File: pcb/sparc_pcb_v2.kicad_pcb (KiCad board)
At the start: 2 copper layers, 36.5 x 36.5 mm, 19 parts, among them SW4 Reset, SW5 BOOT, U2 ESP32-WROOM-32

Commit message: placing C8, R8, and R9
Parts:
- added C8: 1µF, Capacitor_SMD:C_1206_3216Metric_Pad1.33x1.80mm_HandSolder, B.Cu at (144.4, 77.5)
- added R8: 4.7k, Resistor_SMD:R_1206_3216Metric_Pad1.30x1.75mm_HandSolder, B.Cu at (122.0, 98.5)
- added R9: 4.7k, Resistor_SMD:R_1206_3216Metric_Pad1.30x1.75mm_HandSolder, B.Cu at (121.5, 95.0)
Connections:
- LDO1 pad 3: unconnected-(LDO1-EN-Pad3) -> TP4056 OUT+
- SW4 pad 2: +3.3V -> Net-(U2-EN)
- SW5 pad 2: +3.3V -> Net-(U2-IO0)
- VL53L0X1 pad 3: Net-(U2-IO16) -> Net-(U2-IO17)
- VL53L0X1 pad 4: Net-(U2-IO17) -> Net-(U2-IO16)

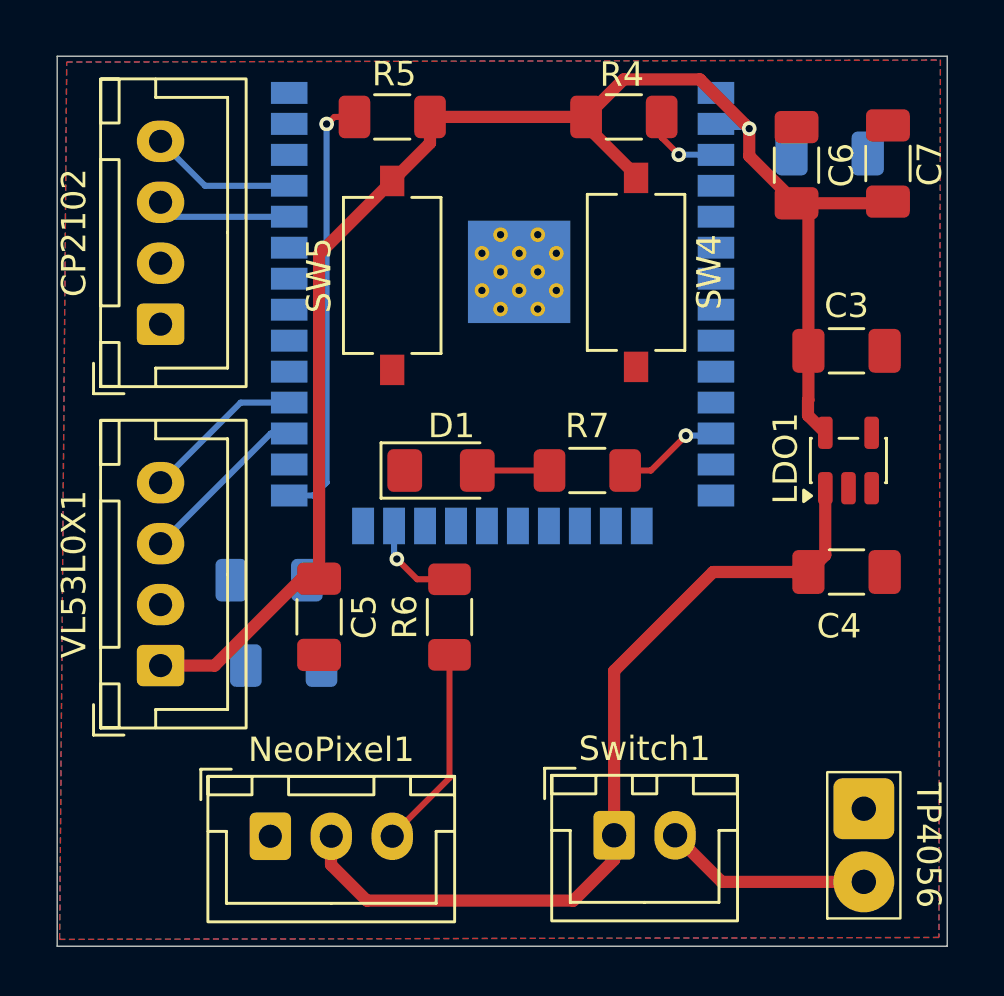
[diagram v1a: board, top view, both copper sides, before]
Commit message: fixed sw4 and sw5 wiring on the pcb
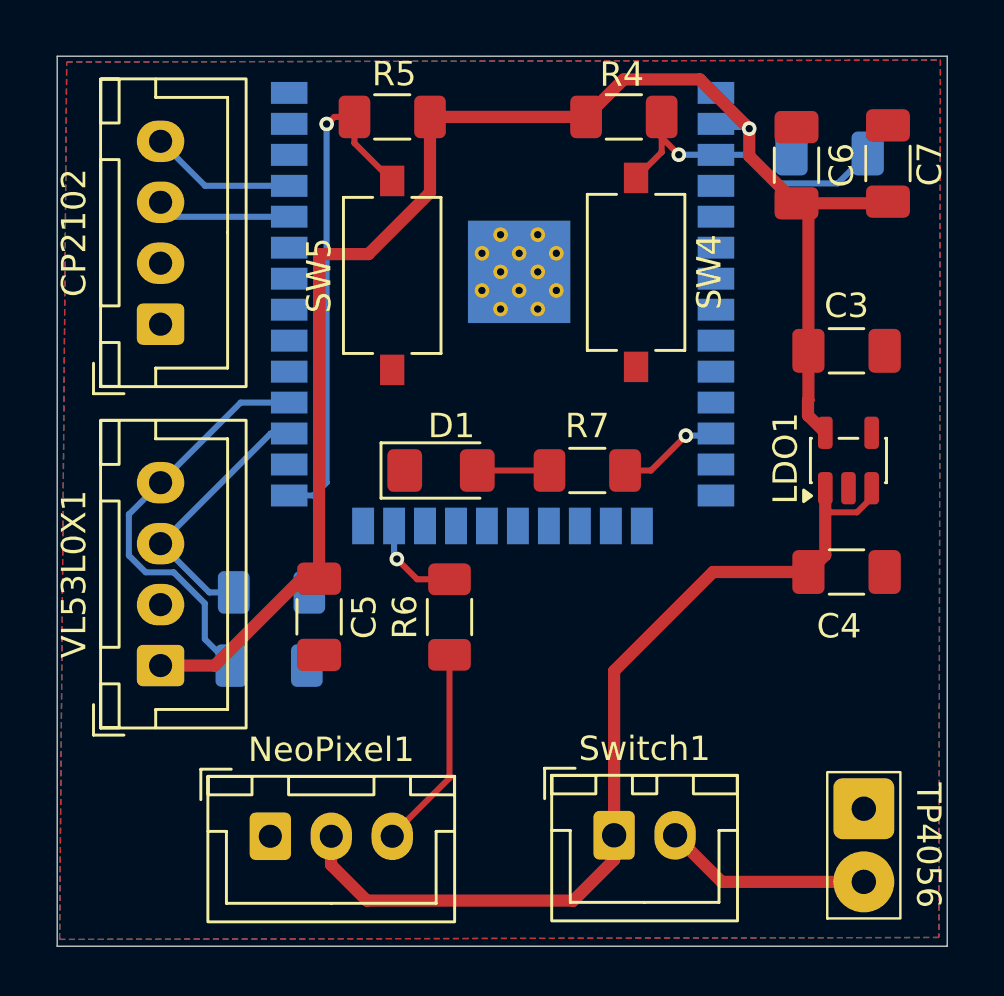
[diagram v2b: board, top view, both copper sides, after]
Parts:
- moved R8 0.60 mm to (121.5, 98.5)
- moved R9 0.51 mm to (121.5, 95.5)
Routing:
- net Net-(U2-IO16): track 7.15 -> 17.1 mm
- net Net-(U2-EN): track 3.57 -> 13.0 mm
- net TP4056 OUT+: track 35.2 -> 38.6 mm
- net Net-(U2-IO17): track 6.64 -> 10.0 mm
- net Net-(U2-IO0): track 18.0 -> 20.7 mm
- net +3.3V: track 65.7 -> 63.9 mm
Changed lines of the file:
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@@
 	(footprint "Resistor_SMD:R_1206_3216Metric_Pad1.30x1.75mm_HandSolder"
 		(layer "B.Cu")
-		(at 121.45 95 180)
+		(at 121.55 95.5 180)
 		(descr "Resistor SMD 1206 (3216 Metric), square (rectangular) end terminal, IPC-7351 nominal with elongated pad for handsoldering. (Body size source: IPC-SM-782 page 72, https://www.pcb-3d.com/wordpress/wp-content/uploads/ipc-sm-782a_amendment_1_and_2.pdf)")
 		(tags "resistor handsolder")
@@
 	(footprint "Resistor_SMD:R_1206_3216Metric_Pad1.30x1.75mm_HandSolder"
 		(layer "B.Cu")
-		(at 122.05 98.5 180)
+		(at 121.45 98.5 180)
 		(descr "Resistor SMD 1206 (3216 Metric), square (rectangular) end terminal, IPC-7351 nominal with elongated pad for handsoldering. (Body size source: IPC-SM-782 page 72, https://www.pcb-3d.com/wordpress/wp-content/uploads/ipc-sm-782a_amendment_1_and_2.pdf)")
 		(tags "resistor handsolder")
@@
 	)
 	(segment
+		(start 128.05 79.1)
+		(end 125.525 81.625)
+		(width 0.5)
+		(layer "F.Cu")
+		(net "+3.3V")
+	)
+	(segment
 		(start 144.26 88.9525)
 		(end 143.55 88.2425)
@@
 	)
 	(segment
-		(start 128.05 77.075)
-		(end 126.5 78.625)
-		(width 0.5)
-		(layer "F.Cu")
-		(net "+3.3V")
-	)
-	(segment
 		(start 143.5675 80.03)
 		(end 143.08 79.5425)
@@
 	)
 	(segment
-		(start 128.05 76)
-		(end 128.05 77.075)
-		(width 0.5)
-		(layer "F.Cu")
-		(net "+3.3V")
-	)
-	(segment
 		(start 122.7825 94.9375)
 		(end 119.22 98.5)
@@
 	)
 	(segment
-		(start 126.5 78.625)
-		(end 123.5 81.625)
-		(width 0.5)
-		(layer "F.Cu")
-		(net "+3.3V")
-	)
-	(segment
 		(start 146.76 79.5425)
 		(end 146.83 79.4725)
@@
 	)
 	(segment
-		(start 136.48 78.38)
-		(end 134.45 76.35)
-		(width 0.5)
-		(layer "F.Cu")
-		(net "+3.3V")
-	)
-	(segment
-		(start 136.48 78.48)
-		(end 136.48 78.38)
-		(width 0.25)
+		(start 125.525 81.625)
+		(end 123.5 81.625)
+		(width 0.5)
 		(layer "F.Cu")
 		(net "+3.3V")
@@
 	)
 	(segment
+		(start 128.05 76)
+		(end 128.05 79.1)
+		(width 0.5)
+		(layer "F.Cu")
+		(net "+3.3V")
+	)
+	(segment
 		(start 135.988279 74.461721)
 		(end 139.121721 74.461721)
@@
 		(end 117 98.5)
 		(width 0.5)
-		(layer "F.Cu")
-		(net "+3.3V")
-	)
-	(segment
-		(start 136.5 78.5)
-		(end 136.48 78.48)
-		(width 0.25)
 		(layer "F.Cu")
 		(net "+3.3V")
@@
 	)
 	(segment
+		(start 144.26 92)
+		(end 144.26 91.2275)
+		(width 0.25)
+		(layer "F.Cu")
+		(net "TP4056 OUT+")
+	)
+	(segment
 		(start 133.93 108.14)
 		(end 125.46 108.14)
@@
 	)
 	(segment
+		(start 146.16 91.615908)
+		(end 145.560908 92.215)
+		(width 0.25)
+		(layer "F.Cu")
+		(net "TP4056 OUT+")
+	)
+	(segment
+		(start 146.16 91.2275)
+		(end 146.16 91.615908)
+		(width 0.25)
+		(layer "F.Cu")
+		(net "TP4056 OUT+")
+	)
+	(segment
 		(start 143.5675 94.6625)
 		(end 139.6575 94.6625)
@@
 	)
 	(segment
+		(start 144.475 92.215)
+		(end 144.26 92)
+		(width 0.25)
+		(layer "F.Cu")
+		(net "TP4056 OUT+")
+	)
+	(segment
 		(start 135.6 106.47)
 		(end 133.93 108.14)
@@
 	)
 	(segment
+		(start 145.560908 92.215)
+		(end 144.475 92.215)
+		(width 0.25)
+		(layer "F.Cu")
+		(net "TP4056 OUT+")
+	)
+	(segment
 		(start 135.6 98.72)
 		(end 135.6 105.46)
@@
 	)
 	(segment
+		(start 136.48 78.48)
+		(end 136.48 78.38)
+		(width 0.25)
+		(layer "F.Cu")
+		(net "Net-(U2-EN)")
+	)
+	(segment
+		(start 136.5 78.5)
+		(end 137.55 77.45)
+		(width 0.25)
+		(layer "F.Cu")
+		(net "Net-(U2-EN)")
+	)
+	(segment
+		(start 137.55 77.45)
+		(end 137.55 76.85)
+		(width 0.25)
+		(layer "F.Cu")
+		(net "Net-(U2-EN)")
+	)
+	(segment
 		(start 137.55 76.85)
 		(end 138.25 77.55)
+		(width 0.25)
+		(layer "F.Cu")
+		(net "Net-(U2-EN)")
+	)
+	(segment
+		(start 136.5 78.5)
+		(end 136.48 78.48)
 		(width 0.25)
 		(layer "F.Cu")
@@
 	)
 	(segment
+		(start 141.0474 77.555)
+		(end 139.775 77.555)
+		(width 0.25)
+		(layer "B.Cu")
+		(net "Net-(U2-EN)")
+	)
+	(segment
 		(start 139.77 77.55)
 		(end 139.775 77.555)
@@
 		(start 138.25 77.55)
 		(end 139.77 77.55)
+		(width 0.25)
+		(layer "B.Cu")
+		(net "Net-(U2-EN)")
+	)
+	(segment
+		(start 144.775 78.725)
+		(end 142.2174 78.725)
+		(width 0.25)
+		(layer "B.Cu")
+		(net "Net-(U2-EN)")
+	)
+	(segment
+		(start 142.2174 78.725)
+		(end 141.0474 77.555)
+		(width 0.25)
+		(layer "B.Cu")
+		(net "Net-(U2-EN)")
+	)
+	(segment
+		(start 146 77.5)
+		(end 144.775 78.725)
 		(width 0.25)
 		(layer "B.Cu")
@@
 	)
 	(segment
+		(start 119.9 98.5)
+		(end 118.813604 97.413604)
+		(width 0.25)
+		(layer "B.Cu")
+		(net "Net-(U2-IO16)")
+	)
+	(segment
+		(start 117.538604 94.675)
+		(end 116.388299 94.675)
+		(width 0.25)
+		(layer "B.Cu")
+		(net "Net-(U2-IO16)")
+	)
+	(segment
+		(start 115.7 93.986701)
+		(end 115.7 92.3)
+		(width 0.25)
+		(layer "B.Cu")
+		(net "Net-(U2-IO16)")
+	)
+	(segment
+		(start 115.7 92.3)
+		(end 116.681802 91.318198)
+		(width 0.25)
+		(layer "B.Cu")
+		(net "Net-(U2-IO16)")
+	)
+	(segment
+		(start 118.813604 95.95)
+		(end 117.538604 94.675)
+		(width 0.25)
+		(layer "B.Cu")
+		(net "Net-(U2-IO16)")
+	)
+	(segment
 		(start 117 93.5)
 		(end 121.515 88.985)
@@
 	)
 	(segment
+		(start 116.388299 94.675)
+		(end 115.7 93.986701)
+		(width 0.25)
+		(layer "B.Cu")
+		(net "Net-(U2-IO16)")
+	)
+	(segment
+		(start 118.813604 97.413604)
+		(end 118.813604 95.95)
+		(width 0.25)
+		(layer "B.Cu")
+		(net "Net-(U2-IO16)")
+	)
+	(segment
 		(start 117 91)
 		(end 120.285 87.715)
@@
 	)
 	(segment
+		(start 119 95.5)
+		(end 117.318198 93.818198)
+		(width 0.25)
+		(layer "B.Cu")
+		(net "Net-(U2-IO17)")
+	)
+	(segment
 		(start 120.285 87.715)
 		(end 122.275 87.715)
+		(width 0.25)
+		(layer "B.Cu")
+		(net "Net-(U2-IO17)")
+	)
+	(segment
+		(start 120 95.5)
+		(end 119 95.5)
 		(width 0.25)
 		(layer "B.Cu")
@@
 	)
 	(segment
+		(start 124.95 77.075)
+		(end 126.093414 78.218414)
+		(width 0.25)
+		(layer "F.Cu")
+		(net "Net-(U2-IO0)")
+	)
+	(segment
 		(start 123.81 76.29)
 		(end 123.81 76.32)
@@
 		(width 0.25)
 		(layer "F.Cu")
+		(net "Net-(U2-IO0)")
+	)
+	(segment
+		(start 124.95 76)
+		(end 124.95 77.075)
+		(width 0.25)
+		(layer "F.Cu")

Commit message: new I2C tracing and pull-up resistors
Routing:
- net Net-(U2-IO17): track 10.0 -> 32.3 mm
- net +3.3V: track 63.9 -> 70.1 mm, vias 1 -> 2
- net Net-(U2-IO16): track 17.1 -> 16.1 mm
- net Net-(U2-IO0): track 20.7 -> 21.3 mm
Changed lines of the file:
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@@
 	)
 	(segment
-		(start 123.5 81.625)
+		(start 123.5 92.5)
 		(end 123.5 94.9375)
 		(width 0.5)
@@
 	)
 	(segment
+		(start 123.5 81.625)
+		(end 123.5 92.5)
+		(width 0.5)
+		(layer "F.Cu")
+		(net "+3.3V")
+	)
+	(segment
 		(start 123.5 94.9375)
 		(end 122.7825 94.9375)
@@
 		(width 0.5)
 		(layer "F.Cu")
+		(net "+3.3V")
+	)
+	(via
+		(at 123.5 92.5)
+		(size 0.6)
+		(drill 0.3)
+		(layers "F.Cu" "B.Cu")
 		(net "+3.3V")
 	)
@@
 	)
 	(segment
+		(start 123 95.6)
+		(end 123.1 95.5)
+		(width 0.25)
+		(layer "B.Cu")
+		(net "+3.3V")
+	)
+	(segment
+		(start 123 98.5)
+		(end 123 95.6)
+		(width 0.25)
+		(layer "B.Cu")
+		(net "+3.3V")
+	)
+	(segment
 		(start 140.945 76.285)
 		(end 141.14 76.48)
+		(width 0.25)
+		(layer "B.Cu")
+		(net "+3.3V")
+	)
+	(segment
+		(start 123.1 95.5)
+		(end 123.1 92.9)
+		(width 0.25)
+		(layer "B.Cu")
+		(net "+3.3V")
+	)
+	(segment
+		(start 123.1 92.9)
+		(end 123.5 92.5)
 		(width 0.25)
 		(layer "B.Cu")
@@
 	)
 	(segment
+		(start 124.95 77.075)
+		(end 126.5 78.625)
+		(width 0.25)
+		(layer "F.Cu")
+		(net "Net-(U2-IO0)")
+	)
+	(segment
+		(start 123.81 76.29)
+		(end 123.81 76.32)
+		(width 0.25)
+		(layer "F.Cu")
+		(net "Net-(U2-IO0)")
+	)
+	(segment
+		(start 123.82 76.33)
+		(end 123.82 76.31)
+		(width 0.25)
+		(layer "F.Cu")
+		(net "Net-(U2-IO0)")
+	)
+	(segment
+		(start 124.13 76)
+		(end 124.95 76)
+		(width 0.25)
+		(layer "F.Cu")
+		(net "Net-(U2-IO0)")
+	)
+	(segment
+		(start 123.82 76.31)
+		(end 124.13 76)
+		(width 0.25)
+		(layer "F.Cu")
+		(net "Net-(U2-IO0)")
+	)
+	(segment
+		(start 124.95 76)
+		(end 124.95 77.075)
+		(width 0.25)
+		(layer "F.Cu")
+		(net "Net-(U2-IO0)")
+	)
+	(segment
+		(start 123.81 76.32)
+		(end 123.82 76.33)
+		(width 0.25)
+		(layer "F.Cu")
+		(net "Net-(U2-IO0)")
+	)
+	(via
+		(at 123.81 76.29)
+		(size 0.6)
+		(drill 0.3)
+		(layers "F.Cu" "B.Cu")
+		(net "Net-(U2-IO0)")
+	)
+	(segment
+		(start 123.81 90.99)
+		(end 123.275 91.525)
+		(width 0.25)
+		(layer "B.Cu")
+		(net "Net-(U2-IO0)")
+	)
+	(segment
+		(start 123.81 76.29)
+		(end 123.81 90.99)
+		(width 0.25)
+		(layer "B.Cu")
+		(net "Net-(U2-IO0)")
+	)
+	(segment
+		(start 122.42 91.38)
+		(end 122.275 91.525)
+		(width 0.25)
+		(layer "B.Cu")
+		(net "Net-(U2-IO0)")
+	)
+	(segment
+		(start 123.275 91.525)
+		(end 122.275 91.525)
+		(width 0.25)
+		(layer "B.Cu")
+		(net "Net-(U2-IO0)")
+	)
+	(segment
+		(start 123.81 76.29)
+		(end 123.82 76.3)
+		(width 0.25)
+		(layer "B.Cu")
+		(net "Net-(U2-IO0)")
+	)
+	(segment
+		(start 117.938604 97.175)
+		(end 118.925 98.161396)
+		(width 0.25)
+		(layer "B.Cu")
+		(net "Net-(U2-IO17)")
+	)
+	(segment
+		(start 118.925 98.161396)
+		(end 118.925 99.3701)
+		(width 0.25)
+		(layer "B.Cu")
+		(net "Net-(U2-IO17)")
+	)
+	(segment
+		(start 120.5451 99.7)
+		(end 120.875 99.3701)
+		(width 0.25)
+		(layer "B.Cu")
+		(net "Net-(U2-IO17)")
+	)
+	(segment
+		(start 115.179968 95.966669)
+		(end 116.388299 97.175)
+		(width 0.25)
+		(layer "B.Cu")
+		(net "Net-(U2-IO17)")
+	)
+	(segment
+		(start 119.2549 99.7)
+		(end 120.5451 99.7)
+		(width 0.25)
+		(layer "B.Cu")
+		(net "Net-(U2-IO17)")
+	)
+	(segment
+		(start 119 95.5)
+		(end 117.318198 93.818198)
+		(width 0.25)
+		(layer "B.Cu")
+		(net "Net-(U2-IO17)")
+	)
+	(segment
+		(start 115.179968 91.033331)
+		(end 115.179968 95.966669)
+		(width 0.25)
+		(layer "B.Cu")
+		(net "Net-(U2-IO17)")
+	)
+	(segment
+		(start 120.875 99.3701)
+		(end 120.875 97.375)
+		(width 0.25)
+		(layer "B.Cu")
+		(net "Net-(U2-IO17)")
+	)
+	(segment
+		(start 118.925 99.3701)
+		(end 119.2549 99.7)
+		(width 0.25)
+		(layer "B.Cu")
+		(net "Net-(U2-IO17)")
+	)
+	(segment
+		(start 120.875 97.375)
+		(end 117 93.5)
+		(width 0.25)
+		(layer "B.Cu")
+		(net "Net-(U2-IO17)")
+	)
+	(segment
+		(start 122.275 87.715)
+		(end 118.498299 87.715)
+		(width 0.25)
+		(layer "B.Cu")
+		(net "Net-(U2-IO17)")
+	)
+	(segment
+		(start 118.498299 87.715)
+		(end 115.179968 91.033331)
+		(width 0.25)
+		(layer "B.Cu")
+		(net "Net-(U2-IO17)")
+	)
+	(segment
+		(start 116.388299 97.175)
+		(end 117.938604 97.175)
+		(width 0.25)
+		(layer "B.Cu")
+		(net "Net-(U2-IO17)")
+	)
+	(segment
+		(start 120 95.5)
+		(end 119 95.5)
+		(width 0.25)
+		(layer "B.Cu")
+		(net "Net-(U2-IO17)")
+	)
+	(segment
 		(start 119.9 98.5)
 		(end 118.813604 97.413604)
@@
 	)
 	(segment
+		(start 122.275 88.985)
+		(end 119.015 88.985)
+		(width 0.25)
+		(layer "B.Cu")
+		(net "Net-(U2-IO16)")
+	)
+	(segment
 		(start 115.7 93.986701)
 		(end 115.7 92.3)
@@
 	)
 	(segment
-		(start 117 93.5)
-		(end 121.515 88.985)
-		(width 0.25)
-		(layer "B.Cu")
-		(net "Net-(U2-IO16)")
-	)
-	(segment
-		(start 121.515 88.985)
-		(end 122.275 88.985)
-		(width 0.25)
-		(layer "B.Cu")
-		(net "Net-(U2-IO16)")
-	)
-	(segment
 		(start 116.388299 94.675)
 		(end 115.7 93.986701)
@@
 	)
 	(segment
-		(start 117 91)
-		(end 120.285 87.715)
-		(width 0.25)
-		(layer "B.Cu")
-		(net "Net-(U2-IO17)")
-	)
-	(segment
-		(start 119 95.5)
-		(end 117.318198 93.818198)
-		(width 0.25)
-		(layer "B.Cu")
-		(net "Net-(U2-IO17)")
-	)
-	(segment
-		(start 120.285 87.715)
-		(end 122.275 87.715)
-		(width 0.25)
-		(layer "B.Cu")
-		(net "Net-(U2-IO17)")
-	)
-	(segment
-		(start 120 95.5)
-		(end 119 95.5)
-		(width 0.25)
-		(layer "B.Cu")
-		(net "Net-(U2-IO17)")
+		(start 119.015 88.985)
+		(end 117 91)
+		(width 0.25)
+		(layer "B.Cu")
+		(net "Net-(U2-IO16)")
 	)
 	(segment
@@
 		(net "Net-(U2-IO27)")
 	)
-	(segment
-		(start 124.95 77.075)
-		(end 126.093414 78.218414)
-		(width 0.25)
-		(layer "F.Cu")
-		(net "Net-(U2-IO0)")
-	)
-	(segment
-		(start 123.81 76.29)
-		(end 123.81 76.32)
-		(width 0.25)
-		(layer "F.Cu")
-		(net "Net-(U2-IO0)")
-	)
-	(segment
-		(start 123.82 76.33)
-		(end 123.82 76.31)
-		(width 0.25)
-		(layer "F.Cu")
-		(net "Net-(U2-IO0)")
-	)
-	(segment
-		(start 124.13 76)
-		(end 124.95 76)
-		(width 0.25)
-		(layer "F.Cu")
-		(net "Net-(U2-IO0)")
-	)
-	(segment
-		(start 123.82 76.31)
-		(end 124.13 76)
-		(width 0.25)
-		(layer "F.Cu")
-		(net "Net-(U2-IO0)")
-	)
-	(segment
-		(start 123.81 76.32)
-		(end 123.82 76.33)
-		(width 0.25)
-		(layer "F.Cu")
-		(net "Net-(U2-IO0)")
-	)
-	(segment
-		(start 124.95 76)
-		(end 124.95 77.075)
-		(width 0.25)
-		(layer "F.Cu")
-		(net "Net-(U2-IO0)")
-	)
-	(via
-		(at 123.81 76.29)
-		(size 0.6)
-		(drill 0.3)
-		(layers "F.Cu" "B.Cu")
-		(net "Net-(U2-IO0)")
-	)
-	(segment
-		(start 123.81 90.99)
-		(end 123.275 91.525)
-		(width 0.25)
-		(layer "B.Cu")
-		(net "Net-(U2-IO0)")
-	)
-	(segment
-		(start 123.81 76.29)
-		(end 123.81 90.99)
-		(width 0.25)
-		(layer "B.Cu")
-		(net "Net-(U2-IO0)")
-	)
-	(segment
-		(start 122.42 91.38)
-		(end 122.275 91.525)
-		(width 0.25)
-		(layer "B.Cu")
-		(net "Net-(U2-IO0)")
-	)
-	(segment
-		(start 123.275 91.525)
-		(end 122.275 91.525)
-		(width 0.25)
-		(layer "B.Cu")
-		(net "Net-(U2-IO0)")
-	)
-	(segment
-		(start 123.81 76.29)
-		(end 123.82 76.3)
-		(width 0.25)
-		(layer "B.Cu")
-		(net "Net-(U2-IO0)")
-	)
 	(zone
